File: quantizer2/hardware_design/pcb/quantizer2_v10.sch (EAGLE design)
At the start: 44 parts, among them IC2 LM4040C10IDBZR, IC3 LM1117DT-3.3_NOPB, IC5 MCP4921T-E_MS, IC7 MCP3204-CI_ST, IC9 TL072CD, U1 LM4040C25IDBZR, Y1 8MHz

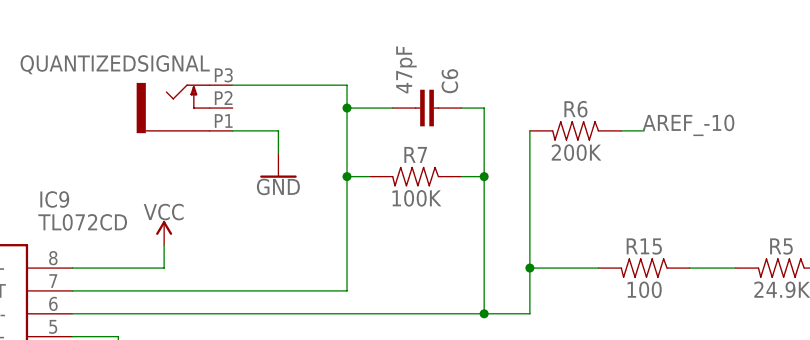
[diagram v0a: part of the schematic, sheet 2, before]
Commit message: design for fet overdrive and quantizer 2 code updates
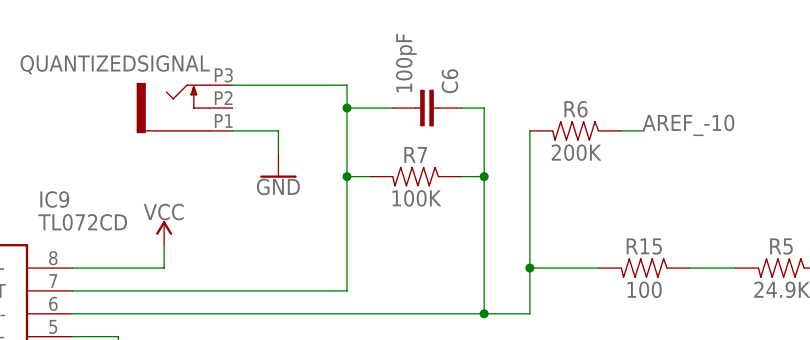
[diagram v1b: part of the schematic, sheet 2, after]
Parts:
- C6: value 47pF -> 100pF
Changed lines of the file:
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@@
 <part name="R15" library="SparkFun-Resistors" library_urn="urn:adsk.eagle:library:532" deviceset="RESISTOR" device="0603" package3d_urn="urn:adsk.eagle:package:39650/1" value="100"/>
 <part name="GND29" library="SparkFun-PowerSymbols" library_urn="urn:adsk.eagle:library:530" deviceset="GND" device=""/>
-<part name="C6" library="SparkFun-Capacitors" library_urn="urn:adsk.eagle:library:510" deviceset="0.1UF" device="-0603-25V-(+80/-20%)" package3d_urn="urn:adsk.eagle:package:37414/1" value="47pF"/>
+<part name="C6" library="SparkFun-Capacitors" library_urn="urn:adsk.eagle:library:510" deviceset="0.1UF" device="-0603-25V-(+80/-20%)" package3d_urn="urn:adsk.eagle:package:37414/1" value="100pF"/>
 </parts>
 <sheets>
